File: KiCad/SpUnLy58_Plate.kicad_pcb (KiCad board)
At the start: 2 copper layers, 318.8 x 137.2 mm, 10 parts

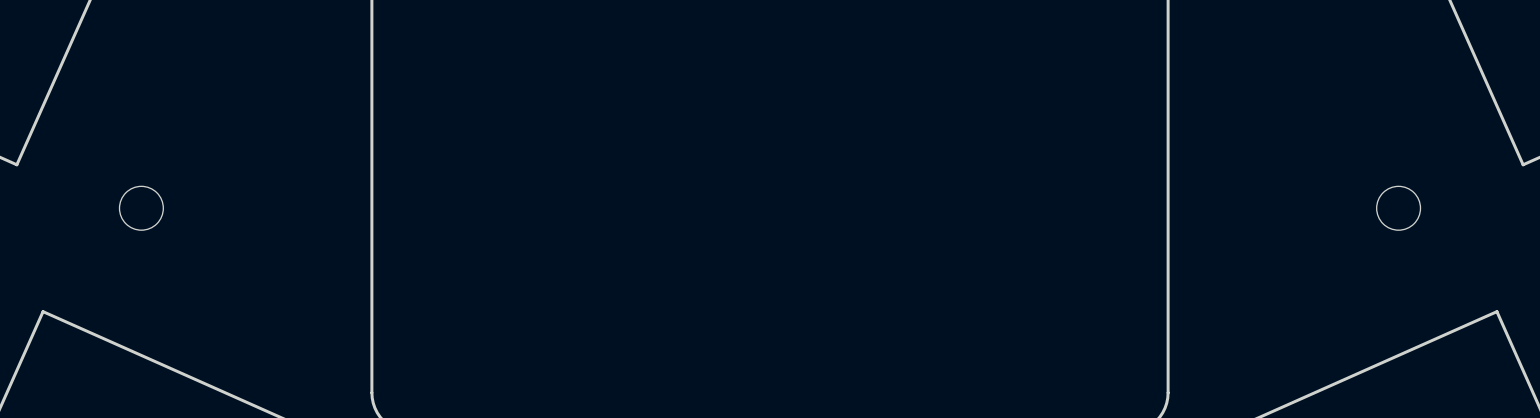
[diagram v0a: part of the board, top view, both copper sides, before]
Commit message: tuned tracks, moved mounting hole.
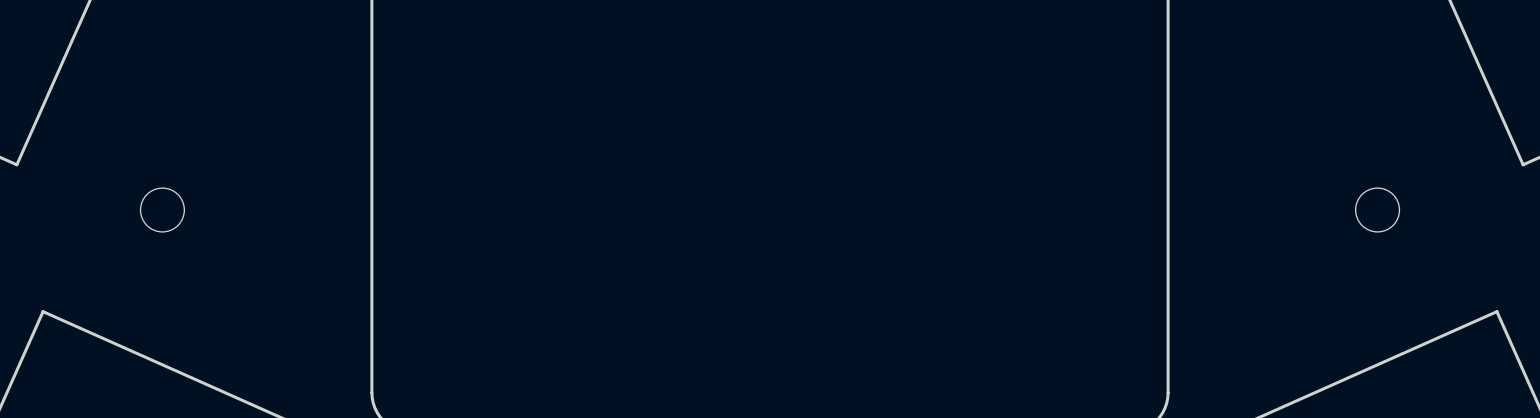
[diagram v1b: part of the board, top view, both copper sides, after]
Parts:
- moved _10 1.06 mm to (239.6, 129.6)
- moved _9 1.06 mm to (178.6, 129.6)
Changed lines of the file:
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@@
       (pad "" np_thru_hole circle (at 0 0) (size 2.2 2.2) (drill 2.2) (layers *.Cu *.Mask F.SilkS) (clearance 0.8)))
       (module HOLE_M2 (layer F.Cu)
-      (at 177.5068429 129.5100011 -24)
+      (at 178.56274620000002 129.5969968 -24)
       (fp_text reference "_9" (at 0 0) (layer Eco2.User) hide (effects (font (size 0.29972 0.29972) (thickness 0.07493))))
       (fp_text value VAL** (at 0 1.75) (layer Eco2.User) hide (effects (font (size 0.29972 0.29972) (thickness 0.07493))))
       (pad "" np_thru_hole circle (at 0 0) (size 2.2 2.2) (drill 2.2) (layers *.Cu *.Mask F.SilkS) (clearance 0.8)))
       (module HOLE_M2 (layer F.Cu)
-      (at 240.62484170000002 129.5100011 24)
+      (at 239.5689384 129.5969968 24)
       (fp_text reference "_10" (at 0 0) (layer Eco2.User) hide (effects (font (size 0.29972 0.29972) (thickness 0.07493))))
       (fp_text value VAL** (at 0 1.75) (layer Eco2.User) hide (effects (font (size 0.29972 0.29972) (thickness 0.07493))))

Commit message: Version 1.0 complete. Finalized routes. Added graphics.
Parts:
- added G***: LOGO, temp:topographic, F.Cu at (288.7, 128.9)
- added G***: LOGO, temp:topographic, F.Cu at (130.0, 128.9)
- _1, _10, _2, _3, _4, _5, _6, _7, _8, _9: value VAL** -> (none)
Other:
- net class Default removed

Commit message: Modified plate cutout from 13.8 to 14mm
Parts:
- removed the G*** at (288.7, 128.9)
- removed the G*** at (130.0, 128.9)
- added G***: LOGO, temp:topographic, F.Cu at (130.0, 141.1)
- added G***: LOGO, temp:topographic, F.Cu at (288.7, 141.1)
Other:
- outline, holes or cut-outs redrawn

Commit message: [v1.1] Reduced vertical spacing from 18 to 17mm Fixed jstph connector footprint and pad label. Increased cutout for battery.
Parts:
- removed the G*** at (130.0, 141.1)
- removed the G*** at (288.7, 141.1)
- added G***: LOGO, temp:topographic, F.Cu at (129.2, 125.9)
- added G***: LOGO, temp:topographic, F.Cu at (287.9, 126.0)
- moved _1 2.99 mm to (102.5, 80.1)
- moved _2 2.92 mm to (314.8, 80.1)
- moved _3 2.85 mm to (154.2, 80.0)
- moved _4 2.85 mm to (263.2, 80.0)
- moved _10 1.00 mm to (239.2, 130.5)
- moved _9 1.00 mm to (178.2, 130.5)
- moved _6 0.81 mm to (320.8, 143.5)
- moved _8 0.76 mm to (249.7, 161.0)
- moved _7 0.50 mm to (167.6, 161.0)
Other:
- board size 318.8 x 137.2 mm -> 318 x 134.4 mm

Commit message: Final v1p2 layout. Update yaml, kicad pcb, and gerber
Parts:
- removed the G*** at (129.2, 125.9)
- removed the G*** at (287.9, 126.0)
- added G***: LOGO, topographic, F.Cu at (287.0, 135.7)
- added G***: LOGO, topographic, F.Cu at (128.3, 135.6)
- moved _9 11.6 mm to (172.4, 120.5), turned to -21 degrees
- moved _10 11.1 mm to (243.9, 120.5), turned to 21 degrees
- moved _3 8.62 mm to (150.2, 72.4)
- moved _4 8.21 mm to (266.2, 72.4)
- moved _8 7.14 mm to (248.0, 154.1), turned to 28 degrees
- moved _7 6.97 mm to (168.3, 154.1), turned to -28 degrees
- moved _1 5.97 mm to (97.6, 76.8), turned to -12 degrees
- moved _2 5.17 mm to (318.8, 76.8), turned to 12 degrees
- moved _6 1.80 mm to (319.7, 142.0), turned to 9 degrees
- moved _5 1.48 mm to (96.6, 142.0), turned to -9 degrees
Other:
- board size 318 x 134.4 mm -> 320.8 x 138.7 mm
